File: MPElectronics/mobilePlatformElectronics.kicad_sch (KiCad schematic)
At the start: 90 parts, among them J1 UART, J2 UART, J3 Magnetic Encoder, J4 Magnetic Encoder, M1 Motor_DC, M2 Motor_DC, M3 Motor_DC, M4 Motor_DC, M5 SG90 9g Micro Servo, M6 RDS51150, M7 RDS51150, M8 SY35ST28-0504A_Stepper_Motor_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, Q1 LTR3208E, SW1 Reset, SW2 Reset, SW3 Reset, SW4 SW_SPDT, SW5 SW_SPDT, SW6 SW_SPDT_LIMIT, SW7 SW_SPDT_LIMIT, U1 PIC32MX170F256B, U10 TLE5206-2S, U12 IR Distance, U13 IR Distance, U14 L293NE/SN754410NE, U2 TLE5206-2S, U3 PIC32MX170F256B, U4 IR Line Sensor, U5 IR Line Sensor, U6 IR Line Sensor, U7 MCP6294, U8 LM339AN, U9 IR Line Sensor

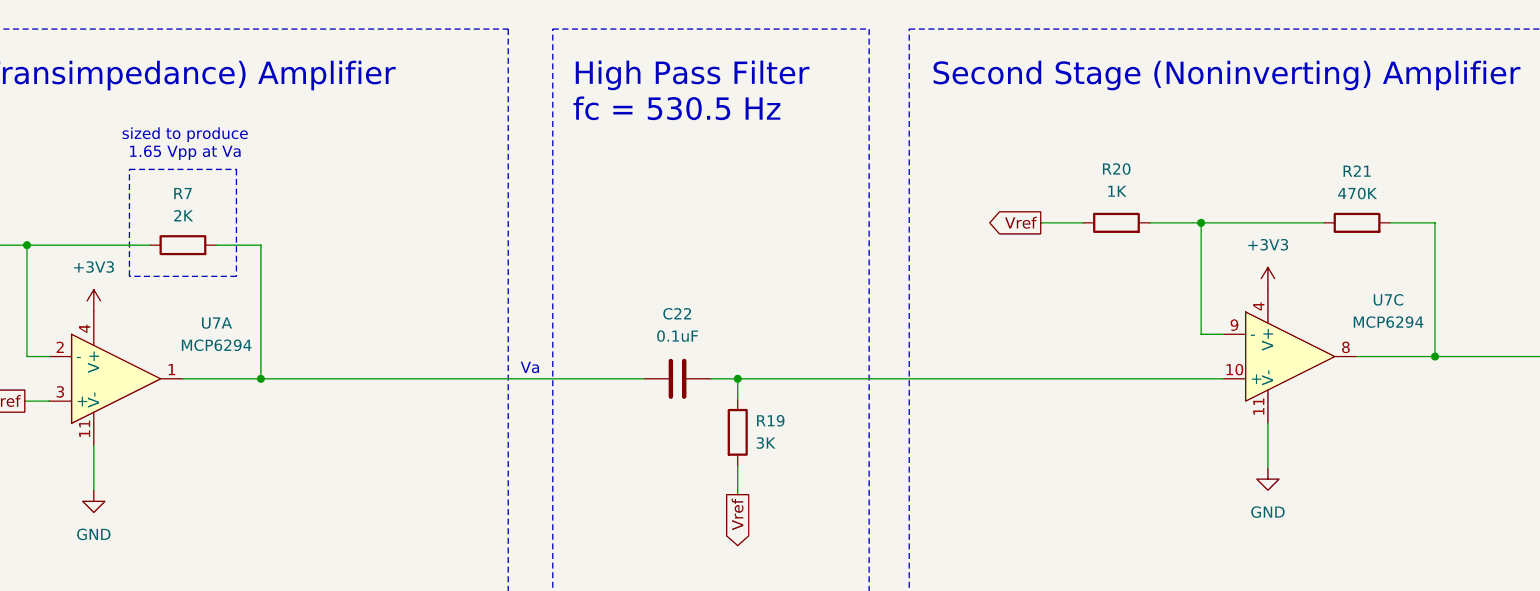
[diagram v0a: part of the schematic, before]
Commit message: updated names of resitors pertaining to the signal conditioning board in kicad to match those in ed's video
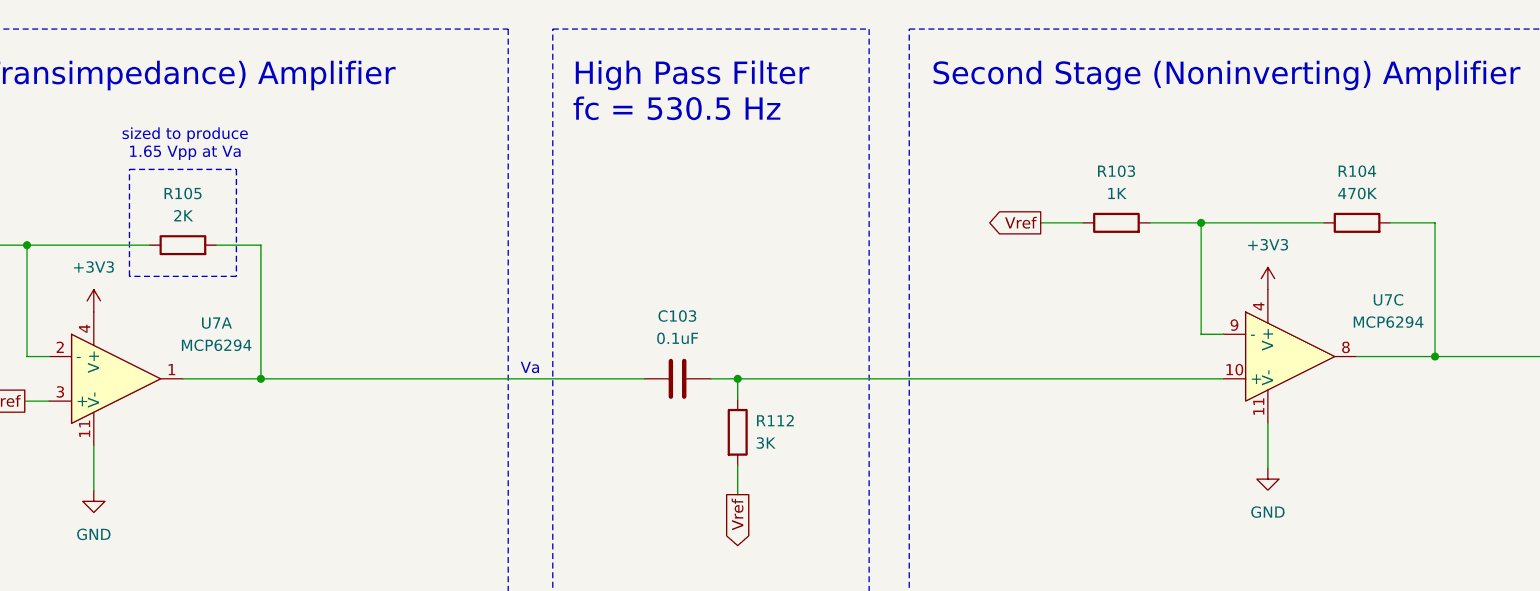
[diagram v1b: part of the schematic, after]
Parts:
- renumbered C22 to C103, R20 to R103, R21 to R104, R7 to R105, R19 to R112
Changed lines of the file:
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@@
 		(dnp no)
 		(fields_autoplaced yes)
-		(property "Reference" "R20"
-			(at 730.758 98.806 90)
+		(property "Reference" "R103"
+			(at 730.758 99.06 90)
 			(effects
 				(font
@@
 		)
 		(property "Value" "1K"
-			(at 730.758 101.346 90)
+			(at 730.758 101.6 90)
 			(effects
 				(font
@@
 			(project "mobilePlatformElectronics"
 				(path "/bd24c4db-4e36-4117-bd4f-5228ef241da9"
-					(reference "R20")
+					(reference "R103")
 					(unit 1)
 				)
@@
 		(dnp no)
 		(fields_autoplaced yes)
-		(property "Reference" "R7"
+		(property "Reference" "R105"
 			(at 624.332 101.6 90)
 			(effects
@@
 			(project "mobilePlatformElectronics"
 				(path "/bd24c4db-4e36-4117-bd4f-5228ef241da9"
-					(reference "R7")
+					(reference "R105")
 					(unit 1)
 				)
@@
 		(dnp no)
 		(fields_autoplaced yes)
-		(property "Reference" "R21"
+		(property "Reference" "R104"
 			(at 758.19 99.06 90)
 			(effects
@@
 			(project "mobilePlatformElectronics"
 				(path "/bd24c4db-4e36-4117-bd4f-5228ef241da9"
-					(reference "R21")
+					(reference "R104")
 					(unit 1)
 				)
@@
 		(dnp no)
 		(fields_autoplaced yes)
-		(property "Reference" "C22"
-			(at 680.72 115.316 90)
+		(property "Reference" "C103"
+			(at 680.72 115.57 90)
 			(effects
 				(font
@@
 		)
 		(property "Value" "0.1uF"
-			(at 680.72 117.856 90)
+			(at 680.72 118.11 90)
 			(effects
 				(font
@@
 			(project "mobilePlatformElectronics"
 				(path "/bd24c4db-4e36-4117-bd4f-5228ef241da9"
-					(reference "C22")
+					(reference "C103")
 					(unit 1)
 				)
@@
 		(dnp no)
 		(fields_autoplaced yes)
-		(property "Reference" "R19"
+		(property "Reference" "R112"
 			(at 689.61 127.5079 0)
 			(effects
@@
 			(project "mobilePlatformElectronics"
 				(path "/bd24c4db-4e36-4117-bd4f-5228ef241da9"
-					(reference "R19")
+					(reference "R112")
 					(unit 1)
 				)

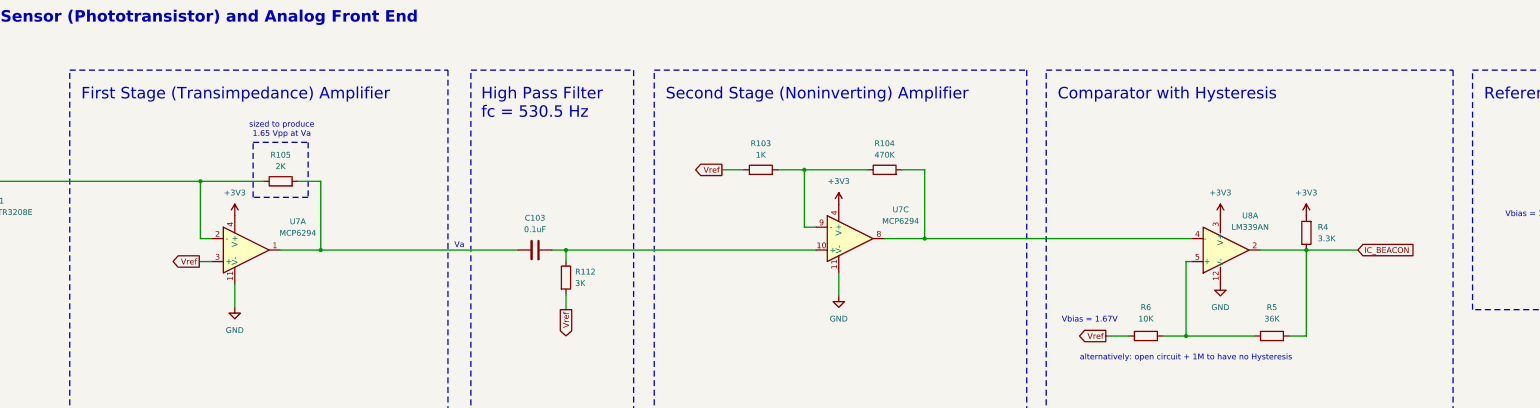
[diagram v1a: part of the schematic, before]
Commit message: updated signal conditioning schematic with resistor names and stage names
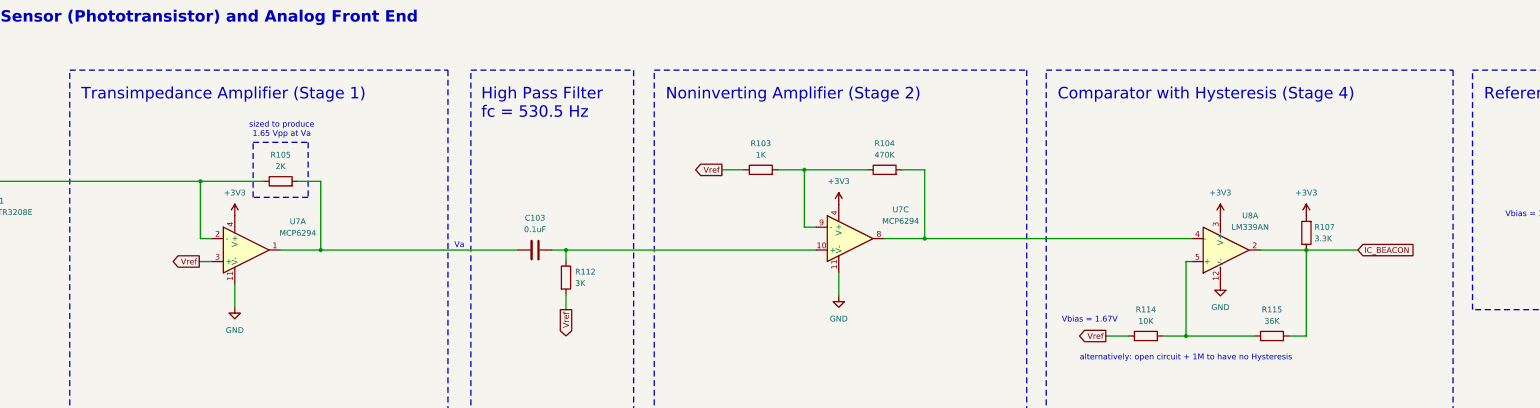
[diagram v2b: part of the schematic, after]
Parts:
- renumbered R4 to R107, R6 to R114, R5 to R115
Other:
- note added: "Comparator with Hysteresis (Stage 4)"
- note added: "Noninverting Amplifier (Stage 2)"
- note added: "Transimpedance Amplifier (Stage 1)"
- note removed: "Comparator with Hysteresis"
- note removed: "First Stage (Transimpedance) Amplifier"
- note removed: "Second Stage (Noninverting) Amplifier"
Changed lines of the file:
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@@
 		)
 	)
-	(text "First Stage (Transimpedance) Amplifier"
+	(text "Transimpedance Amplifier (Stage 1)"
 		(exclude_from_sim no)
 		(at 580.136 88.138 0)
@@
 		)
 	)
-	(text "Second Stage (Noninverting) Amplifier"
+	(text "Noninverting Amplifier (Stage 2)"
 		(exclude_from_sim no)
 		(at 709.676 88.138 0)
@@
 		)
 	)
-	(text "Comparator with Hysteresis"
+	(text "Comparator with Hysteresis (Stage 4)\n"
 		(exclude_from_sim no)
 		(at 796.544 88.138 0)
@@
 		(dnp no)
 		(fields_autoplaced yes)
-		(property "Reference" "R4"
-			(at 854.202 117.6019 0)
+		(property "Reference" "R107"
+			(at 853.44 117.6019 0)
 			(effects
 				(font
@@
 		)
 		(property "Value" "3.3K"
-			(at 854.202 120.1419 0)
+			(at 853.44 120.1419 0)
 			(effects
 				(font
@@
 			(project "mobilePlatformElectronics"
 				(path "/bd24c4db-4e36-4117-bd4f-5228ef241da9"
-					(reference "R4")
+					(reference "R107")
 					(unit 1)
 				)
@@
 		(dnp no)
 		(fields_autoplaced yes)
-		(property "Reference" "R6"
-			(at 816.102 135.382 90)
+		(property "Reference" "R114"
+			(at 816.102 135.89 90)
 			(effects
 				(font
@@
 		)
 		(property "Value" "10K"
-			(at 816.102 137.922 90)
+			(at 816.102 138.43 90)
 			(effects
 				(font
@@
 			(project "mobilePlatformElectronics"
 				(path "/bd24c4db-4e36-4117-bd4f-5228ef241da9"
-					(reference "R6")
+					(reference "R114")
 					(unit 1)
 				)
@@
 		(dnp no)
 		(fields_autoplaced yes)
-		(property "Reference" "R5"
-			(at 844.042 135.382 90)
+		(property "Reference" "R115"
+			(at 844.042 135.89 90)
 			(effects
 				(font
@@
 		)
 		(property "Value" "36K"
-			(at 844.042 137.922 90)
+			(at 844.042 138.43 90)
 			(effects
 				(font
@@
 			(project "mobilePlatformElectronics"
 				(path "/bd24c4db-4e36-4117-bd4f-5228ef241da9"
-					(reference "R5")
+					(reference "R115")
 					(unit 1)
 				)
